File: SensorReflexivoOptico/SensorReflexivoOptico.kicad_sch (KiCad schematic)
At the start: 13 parts, among them U1 LM324

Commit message: Atualizei o resistor
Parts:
- R3: value R -> 470
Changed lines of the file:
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@@
 			)
 		)
-		(property "Value" "R"
+		(property "Value" "470"
 			(at 163.83 107.9499 0)
 			(effects

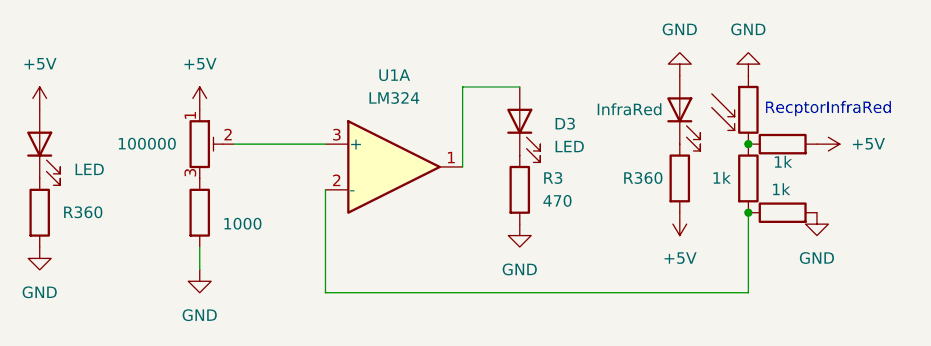
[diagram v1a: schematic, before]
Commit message: Inclusão de alguns modelos de footprint
Resistor - DIN0207 -L6.3mm D2.5mm
LED - LED_D5.0mm_Clear
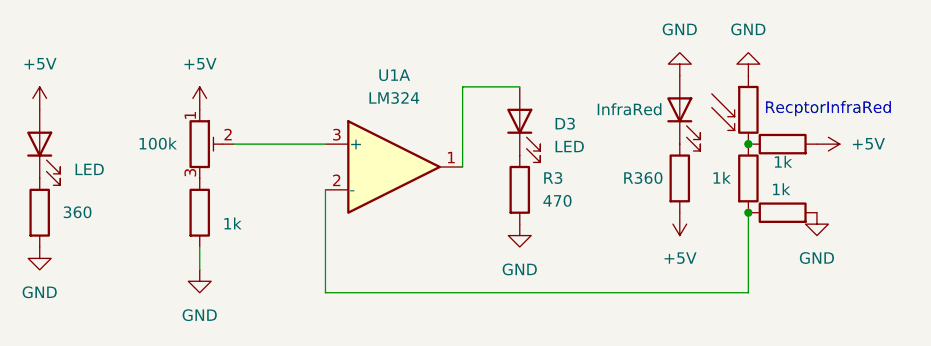
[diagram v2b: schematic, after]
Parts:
- D3: footprint (none) -> LED_THT:LED_D5.0mm_Clear
- R1: value 1000 -> 1k; footprint (none) -> Resistor_THT:R_Axial_DIN0207_L6.3mm_D2.5mm_P10.16mm_Horizontal
- R2: value R360 -> 360
- RV3: value 100000 -> 100k
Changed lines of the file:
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@@
 			)
 		)
-		(property "Value" "100000"
+		(property "Value" "100k"
 			(at 123.19 101.5999 0)
 			(effects
@@
 			)
 		)
-		(property "Value" "1000"
+		(property "Value" "1k"
 			(at 128.27 110.4899 0)
 			(effects
@@
 			)
 		)
-		(property "Footprint" ""
+		(property "Footprint" "Resistor_THT:R_Axial_DIN0207_L6.3mm_D2.5mm_P10.16mm_Horizontal"
 			(at 123.952 109.22 90)
 			(effects
@@
 			)
 		)
-		(property "Footprint" ""
+		(property "Footprint" "LED_THT:LED_D5.0mm_Clear"
 			(at 161.29 99.06 0)
 			(effects
@@
 			)
 		)
-		(property "Value" "R360"
+		(property "Value" "360"
 			(at 110.49 109.2199 0)
 			(effects
